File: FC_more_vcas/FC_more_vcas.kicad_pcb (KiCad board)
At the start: 2 copper layers, 41.4 x 100 mm, 42 parts, among them J1 Con_R, J2 Con_L, J3 Con_Fem_R, J4 Con_Fem_L, J5 Conn_02x05_Odd_Even, Q1 Q_PNP_EBC, Q2 Q_PNP_EBC, U1 LM13700

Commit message: Corrections made after running DRC
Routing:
- net /CV_1: track 29.3 -> 33.4 mm
- net /CV_2: track 48.4 -> 51.2 mm
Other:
- net class Default: trace_width 0.3 -> 0.35

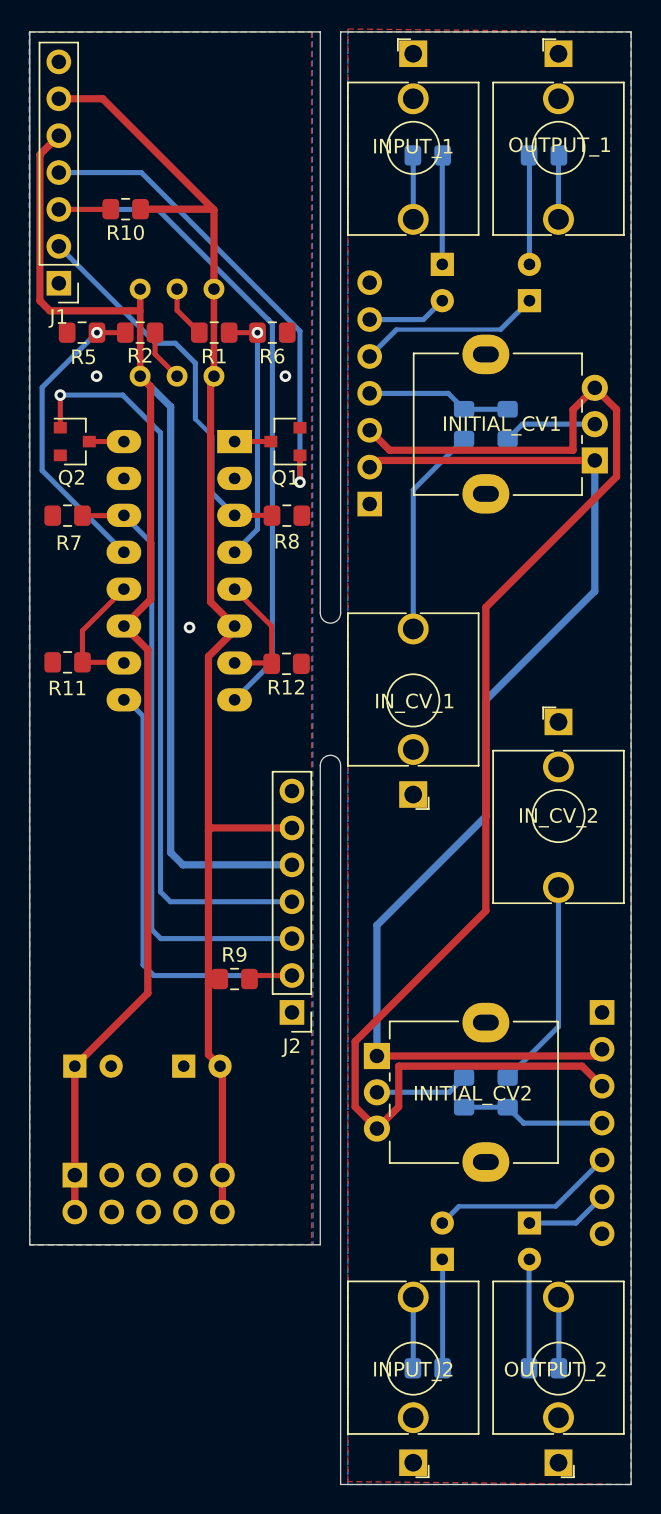
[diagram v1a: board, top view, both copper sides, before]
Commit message: Corrections made to ground planes, trace widths, etc. after visual checks of printout
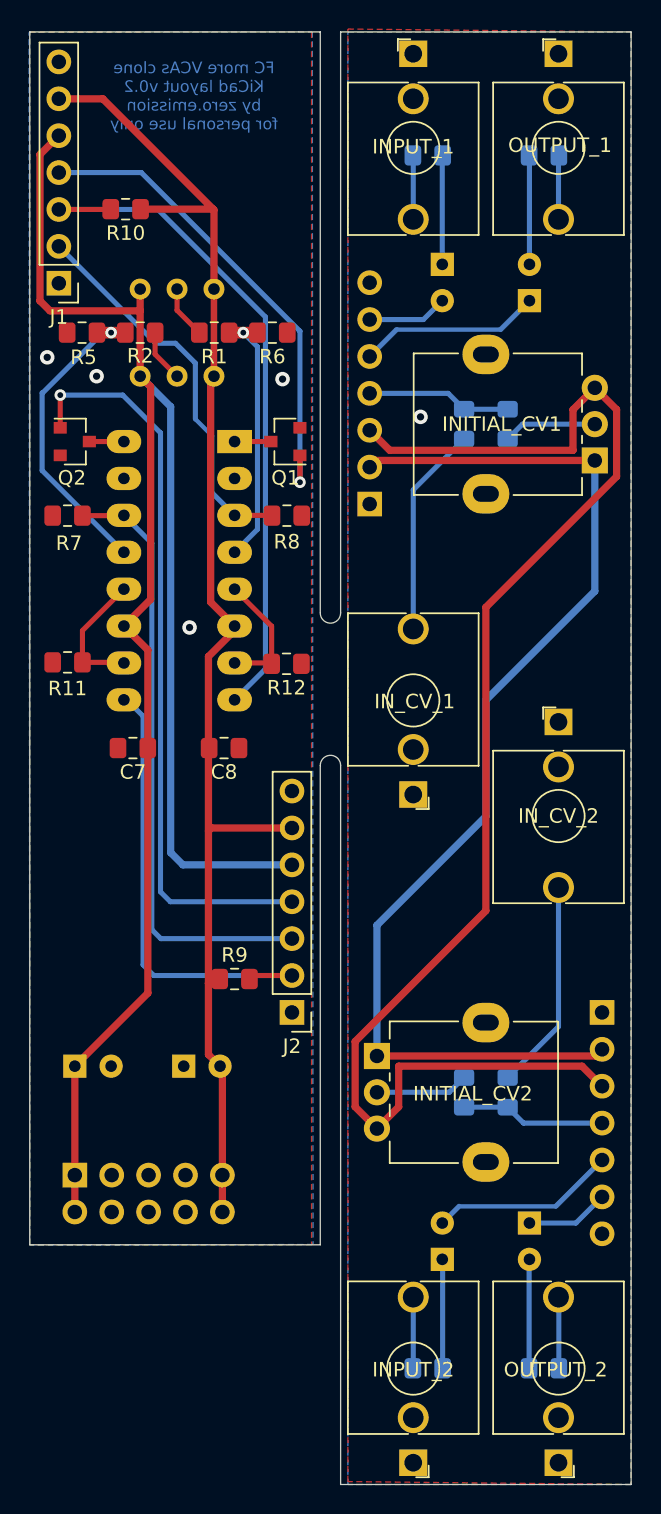
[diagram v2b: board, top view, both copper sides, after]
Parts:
- added C7: 100nF, Capacitor_SMD:C_0805_2012Metric_Pad1.15x1.40mm_HandSolder, F.Cu at (27.2, 68.3)
- added C8: 100nF, Capacitor_SMD:C_0805_2012Metric_Pad1.15x1.40mm_HandSolder, F.Cu at (33.5, 68.3)
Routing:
- net Net-(R2-Pad1): track 21.0 -> 21.7 mm
- net GND: vias 3 -> 4
- net /GND_PNL: vias 0 -> 1
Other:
- net class Power: via_dia 0.8 -> 1; via_drill 0.4 -> 0.5
- board text added: "FC more VCAs clone KiCad layout v0.2 by zero.emission for personal use only"
